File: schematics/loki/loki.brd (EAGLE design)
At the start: 80 x 49 mm, 57 parts, among them IC2 LM358D, Q1 MOSFET-PCHANNELSMD, U1 USD SOCKET, Y1 XRCGB_XTAL

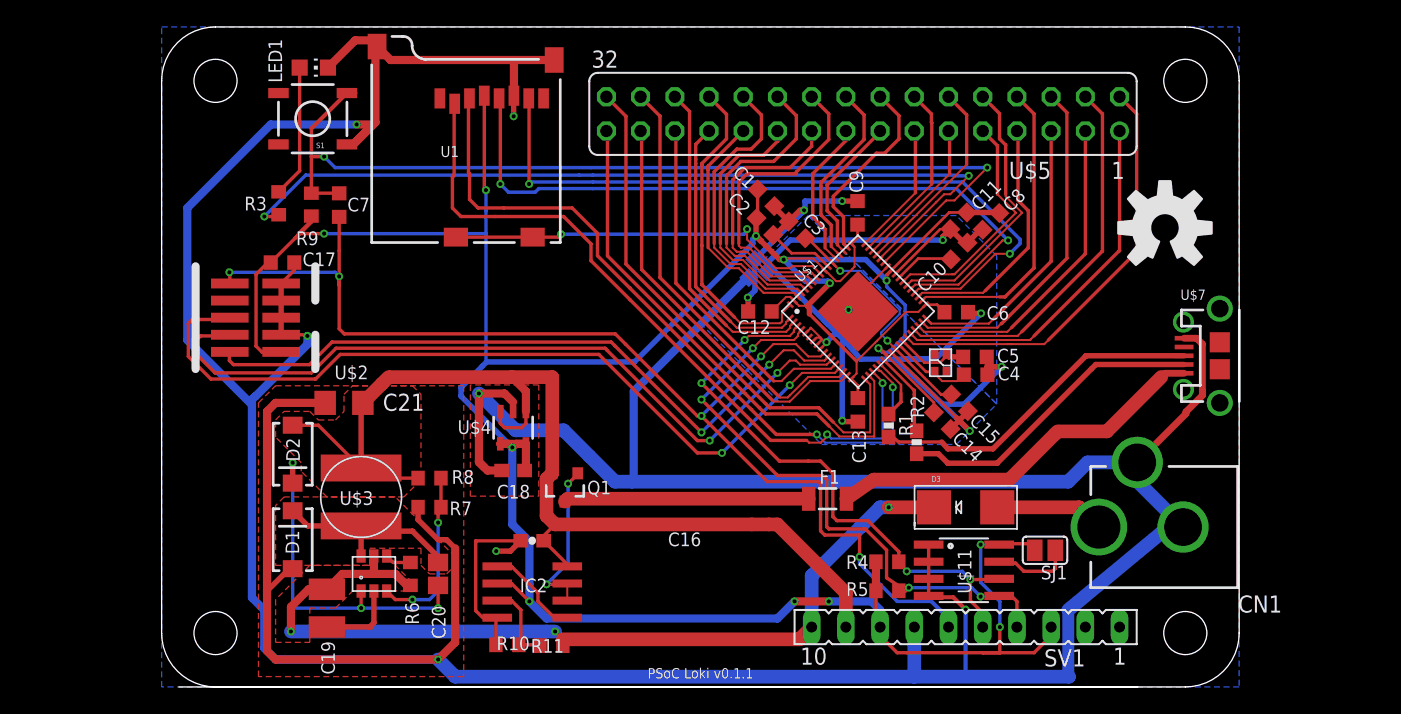
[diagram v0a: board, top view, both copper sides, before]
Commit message: Reworked Loki to fit the 100TQFP package.
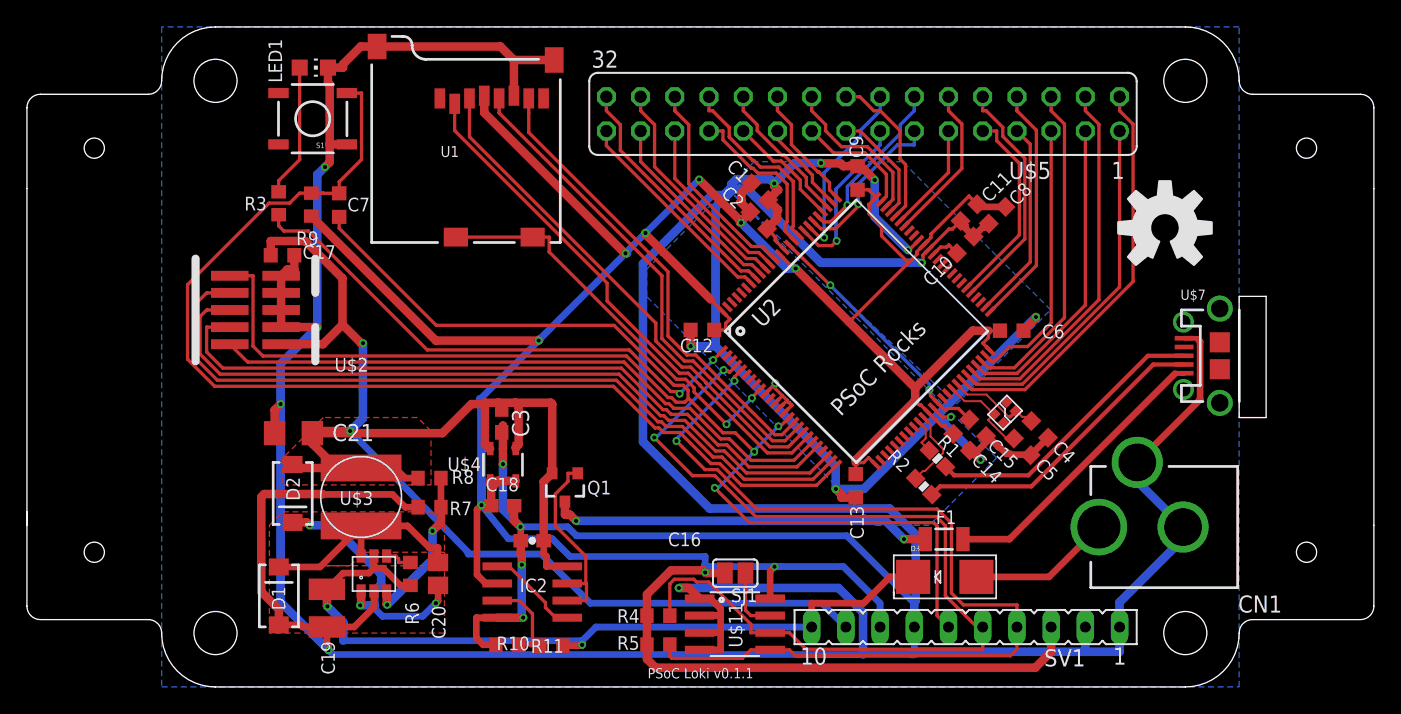
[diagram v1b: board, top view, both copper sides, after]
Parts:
- removed U$1: CY83XXX-68PIN, cypress_psoc_V1_0:QFN68
- removed U$13: (no value), dp_devices:DP8049_V1
- added U2: CY8C5XXX-100PIN, cypress_psoc_V1_0:TQFP-14X14-100
- C3: value 0.1u -> 1u; device resistor:C0603K -> resistor:C0603
- U$9: device SparkFun-Passives:GND_CONNECT -> nickparts:GNDCONNECT
- moved C3 26.1 mm to (25.2, 19.8), turned to 270 degrees
- moved SJ1 23.1 mm to (42.6, 8.45)
- moved R4 17.5 mm to (36.9, 5.29)
- moved R5 17.5 mm to (36.9, 3.14)
- moved U$11 17.5 mm to (42.6, 4.66)
- moved U$6 13.0 mm to (32.8, 25.0)
- moved F1 9.15 mm to (58.1, 11.0)
- moved C5 7.55 mm to (63.9, 17.8), turned to 315 degrees
- moved C4 6.25 mm to (65.2, 19.1), turned to 315 degrees
- moved U$9 6.09 mm to (42.2, 37.0)
- moved Y1 6.05 mm to (62.6, 20.4), turned to 45 degrees
- moved C13 5.64 mm to (51.5, 14.9)
- moved D3 5.39 mm to (58.1, 8.17)
- moved C12 4.48 mm to (40.1, 26.5)
- moved C21 4.37 mm to (9.79, 18.8)
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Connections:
- net N$11 renamed DCIN
- net N$15 renamed VBUS
- net N$2 renamed D-IN
- net N$4 renamed D+IN
- net N$6 renamed BOOST
- net N$7 renamed INDIN
- net N$8 renamed FB
- removed net IND: U$1.P$6
- removed net N$16: C4.1, U$1.P$27, Y1.2
- removed net N$17: C5.1, U$1.P$28, Y1.1
- removed net N$20: C7.1, R9.1, S1.3, U$1.P$46
- removed net P0[0]: U$1.P$48, U$5.12
- removed net P0[1]: U$1.P$49, U$5.11
- removed net P0[2]: U$1.P$50, U$5.14
- removed net P0[3]: U$1.P$51, U$5.13
- removed net P0[4]: U$1.P$53, U$5.16
- removed net P0[5]: U$1.P$54, U$5.15
- removed net P0[6]: U$1.P$55, U$5.18
- removed net P0[7]: U$1.P$56, U$5.17
- removed net P15[2]: U$1.P$40, U$5.10
- removed net P15[3]: U$1.P$41, U$5.9
- removed net P15[5]: U$1.P$61, U$5.20
- removed net P1[2]: U$1.P$13, U$5.27
- removed net P1[4]: U$1.P$15, U$5.30
- removed net P1[6]: U$1.P$18, U$5.32
- removed net P1[7]: U$1.P$19, U$5.31
- removed net P2[0]: U$1.P$62, U$5.19
- removed net P2[1]: U$1.P$63, U$5.22
- removed net P2[2]: U$1.P$64, U$5.21
- removed net P2[3]: U$1.P$65, U$5.24
- removed net P2[4]: U$1.P$66, U$5.23
- removed net P2[5]: U$1.P$68, U$5.26
- removed net P2[6]: U$1.P$1, U$5.25
- removed net P2[7]: U$1.P$2, U$5.28
- removed net P3[0]: U$1.P$29, U$5.2
- removed net P3[1]: U$1.P$30, U$5.1
- removed net P3[2]: U$1.P$31, U$5.4
- removed net P3[3]: U$1.P$32, U$5.3
- removed net P3[4]: U$1.P$33, U$5.6
- removed net P3[5]: U$1.P$34, U$5.5
- removed net P3[6]: U$1.P$36, U$5.8
- removed net P3[7]: U$1.P$37, U$5.7
- new net CLKI: C4.1, U2.43, Y1.2
- new net CLKO: C5.1, U2.42, Y1.1
- new net GPIO1: U$5.2, U2.44
- new net GPIO10: U$5.9, U2.56
- new net GPIO11: U$5.12, U2.69
- new net GPIO12: U$5.11, U2.70
- new net GPIO13: U$5.14, U2.80
- new net GPIO14: U$5.13, U2.81
- new net GPIO15: U$5.16, U2.82
- new net GPIO16: U$5.15, U2.83
- new net GPIO17: U$5.18, U2.71
- new net GPIO18: U$5.17, U2.72
- new net GPIO19: U$5.20, U2.73
- new net GPIO2: U$5.1, U2.45
- new net GPIO20: U$5.19, U2.74
- new net GPIO21: U$5.22, U2.76
- new net GPIO22: U$5.21, U2.77
- new net GPIO23: U$5.24, U2.78
- new net GPIO24: U$5.23, U2.79
- new net GPIO25: U$5.26, U2.84
- new net GPIO26: U$5.25, U2.85
- new net GPIO27: U$5.28, U2.89
- new net GPIO28: U$5.27, U2.90
- new net GPIO29: U$5.30, U2.91
- new net GPIO3: U$5.4, U2.46
- new net GPIO30: U$5.29, U2.92
- new net GPIO31: U$5.32, U2.93
- new net GPIO32: U$5.31, U2.94
- new net GPIO4: U$5.3, U2.47
- new net GPIO5: U$5.6, U2.48
- new net GPIO6: U$5.5, U2.49
- new net GPIO7: U$5.8, U2.51
- new net GPIO8: U$5.7, U2.52
- new net GPIO9: U$5.10, U2.55
- new net N$2: R3.2, U2.1
- new net TDI: U$2.P$8, U2.24
- new net VCCD: C15.1, U2.39, U2.86
- net +3V3: now also U2.100, U2.26, U2.37, U2.50, U2.65, U2.75, U2.88; no longer C17.1, U$1.P$17, U$1.P$24, U$1.P$35, U$1.P$44, U$1.P$52, U$1.P$59, U$1.P$67, U$2.P$1
- net +5V: now also C17.1, C3.1, U$2.P$1
- net AGND: now also U$9.AGND, U2.64; no longer U$1.P$43, U$9.2
- net D+: now also U2.35; no longer U$1.P$22
- net D-: now also U2.36; no longer U$1.P$23
- net DGND: now also U$9.DGND, U2.10, U2.12, U2.13, U2.14, U2.38, U2.66, U2.87; no longer C3.2, U$1.P$25, U$1.P$45, U$1.P$5, U$1.P$58, U$1.P$7, U$1.P$8, U$1.P$9, U$1.P$CENTER, U$9.1
- net GND: now also C3.2, U$9.GND; no longer U$9.3
- net N$1: now also U2.67; no longer C15.1, C3.1, U$1.P$26, U$1.P$57
- net N$10: now also U2.68; no longer R3.2, U$1.P$47
- net N$3: now also U2.63; no longer U$1.P$42
- net P1[5]: now also C7.1, R9.1, S1.3, U2.25; no longer U$1.P$16, U$5.29
- net SCL0: now also U2.4; no longer U$1.P$3
- net SDA0: now also U2.5; no longer U$1.P$4
- net SWDCK: now also U2.21; no longer U$1.P$12
- net SWDIO: now also U2.20; no longer U$1.P$11
- net SWV: now also U2.23; no longer U$1.P$14
- net USD_CD: now also U2.9; no longer U$1.P$60
- net USD_CS: now also U2.19; no longer U$1.P$20
- net USD_DI: now also U2.18; no longer U$1.P$21
- net USD_DO: now also U2.16; no longer U$1.P$38
- net USD_SCK: now also U2.17; no longer U$1.P$39
- net XRES: now also U2.15; no longer U$1.P$10
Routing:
- net N$20: track 72.5 -> 0.00 mm, vias 2 -> 0
- net N$10: track 63.9 -> 0.00 mm, vias 2 -> 0
- net TDI: track 0.00 -> 58.6 mm
- net P1[5]: track 30.5 -> 81.5 mm
- net +5V: track 79.4 -> 124.6 mm, vias 0 -> 2
- net P1[6]: track 40.5 -> 0.00 mm
- net N$2: track 0.00 -> 40.3 mm, vias 0 -> 2
- net P1[7]: track 39.4 -> 0.00 mm
- net P1[4]: track 32.3 -> 0.00 mm
- net P3[0]: track 32.2 -> 0.00 mm
- net GPIO1: track 0.00 -> 30.5 mm
- net P3[2]: track 28.8 -> 0.00 mm
- net SCL0: track 43.7 -> 71.7 mm, vias 4 -> 2
- net GPIO3: track 0.00 -> 27.7 mm
- net P3[1]: track 27.6 -> 0.00 mm
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- removed copper zone on layer 1, net GND
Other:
- board size 80 x 49 mm -> 100 x 49 mm
- board text added: "DP8049_v1"
